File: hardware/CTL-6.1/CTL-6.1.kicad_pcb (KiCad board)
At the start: 2 copper layers, 107.6 x 45.1 mm, 79 parts, among them J1 Conn_02x16_Top_Bottom, J3 Conn_01x03, J4 Conn_01x03, J5 Conn_02x06_Odd_Even, J6 Conn_01x04, J7 Conn_01x04, K1 G5V-1, Q1 BCX56, Q2 BCX56, Q3 BCX56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

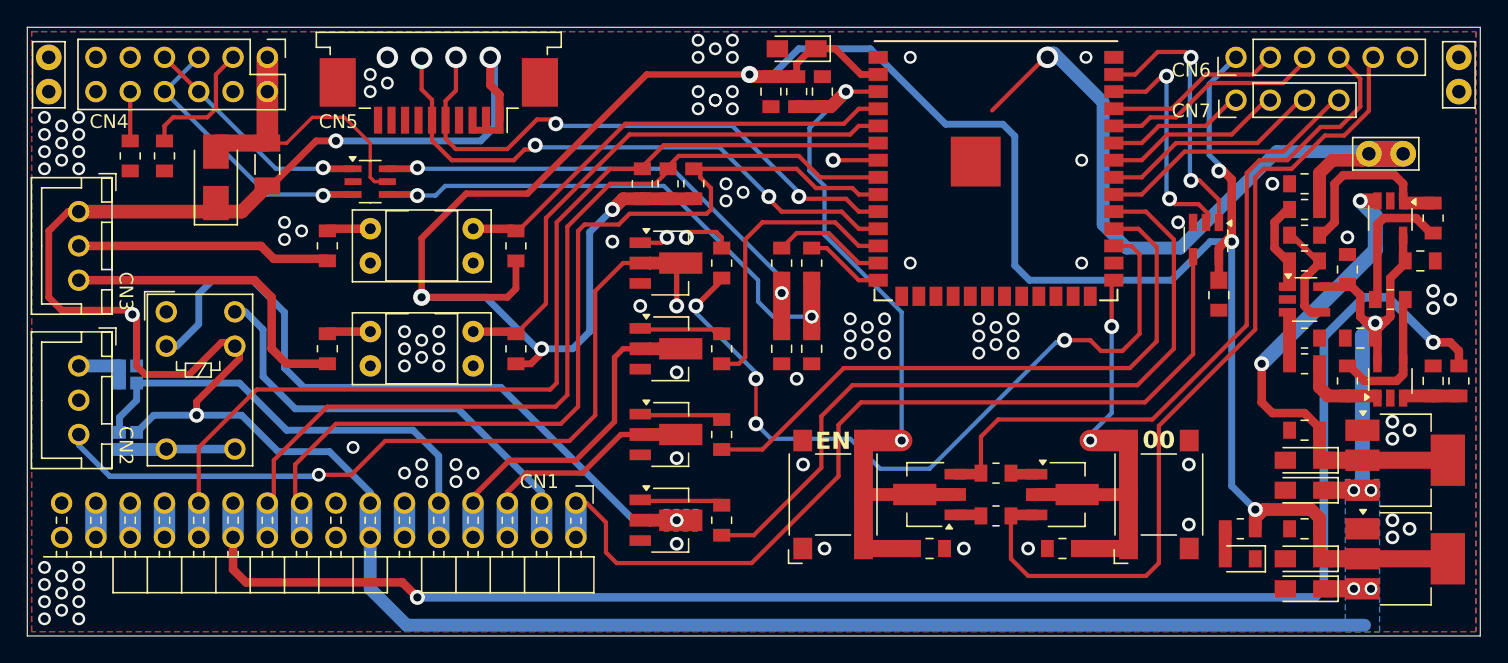
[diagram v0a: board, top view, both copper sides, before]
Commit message: modified:   .DS_Store 	new file:   archive/DL5NEG - Low Cost RF Power Sensor.xlsx 	renamed:    archive/Purchase 20260209/Invoice | Tokopedia 1.pdf -> archive/Purchase 20260209/Invoice - Tokopedia 1.pdf 	renamed:    archive/Purchase 20260209/Invoice | Tokopedia 2.pdf -> archive/Purchase 20260209/Invoice - Tokopedia 2.pdf 	renamed:    archive/Purchase 20260209/Invoice | Tokopedia 3.pdf -> archive/Purchase 20260209/Invoice - Tokopedia 3.pdf 	renamed:    archive/Purchase 20260209/Invoice | Tokopedia 4.pdf -> archive/Purchase 20260209/Invoice - Tokopedia 4.pdf 	renamed:    archive/Purchase 20260209/Invoice | Tokopedia 5.pdf -> archive/Purchase 20260209/Invoice - Tokopedia 5.pdf 	new file:   hardware/CTL-6.1/CTL-6.1-backups/CTL-6.1-2026-05-22_160447.zip 	new file:   hardware/CTL-6.1/CTL-6.1-backups/CTL-6.1-2026-05-22_160956.zip 	new file:   hardware/CTL-6.1/CTL-6.1-backups/CTL-6.1-2026-05-22_162109.zip 	new file:   hardware/CTL-6.1/CTL-6.1-backups/CTL-6.1-2026-05-22_163223.zip 	new file:   hardware/CTL-6.1/CTL-6.1-backups/CTL-6.1-2026-05-22_210324.zip 	new file:   hardware/CTL-6.1/CTL-6.1-backups/CTL-6.1-2026-05-25_112244.zip 	modified:   hardware/CTL-6.1/CTL-6.1.kicad_pcb 	modified:   hardware/CTL-6.1/CTL-6.1.kicad_pro
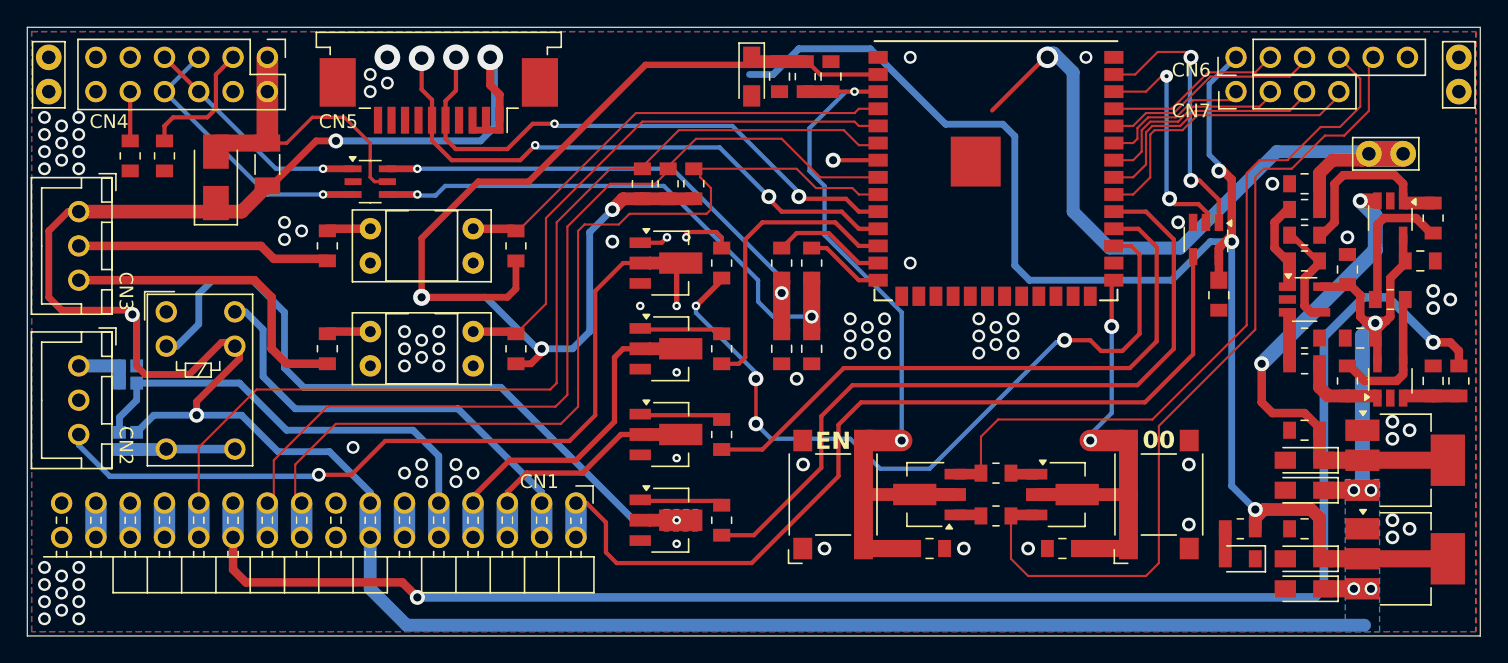
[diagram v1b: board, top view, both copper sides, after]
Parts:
- moved C10 3.92 mm to (98.1, 64.9), turned to -90 degrees
- moved C11 1.28 mm to (100.2, 64.9)
- moved C9 1.28 mm to (104.0, 64.9)
- moved R16 1.28 mm to (102.1, 64.9)
- moved J7 0.63 mm to (134.0, 66.0)
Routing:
- net +3.3V: track 195.4 -> 193.2 mm, vias 7 -> 6
- net /TCK: track 19.5 -> 21.4 mm
- net /TDO: track 16.5 -> 17.9 mm
- net /EN: track 57.3 -> 56.2 mm
- net /MSD2: track 68.5 -> 69.5 mm
- net /TDI: track 13.4 -> 14.3 mm
- net /OPTO: track 73.2 -> 74.1 mm
- net /REM: track 57.2 -> 58.0 mm
- net GND: vias 103 -> 87

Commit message: new file:   hardware/CTL-6.0/CTL-6.0-backups/CTL-6.0-2026-06-11_110233.zip 	modified:   hardware/CTL-6.0/CTL-6.0.kicad_prl 	modified:   hardware/CTL-6.0/CTL-6.0.kicad_pro 	deleted:    hardware/CTL-6.1/CTL-6.1-backups/CTL-6.1-2026-05-21_160708.zip 	deleted:    hardware/CTL-6.1/CTL-6.1-backups/CTL-6.1-2026-05-21_163235.zip 	deleted:    hardware/CTL-6.1/CTL-6.1-backups/CTL-6.1-2026-05-22_160447.zip 	deleted:    hardware/CTL-6.1/CTL-6.1-backups/CTL-6.1-2026-05-22_160956.zip 	deleted:    hardware/CTL-6.1/CTL-6.1-backups/CTL-6.1-2026-05-22_162109.zip 	deleted:    hardware/CTL-6.1/CTL-6.1-backups/CTL-6.1-2026-05-22_163223.zip 	deleted:    hardware/CTL-6.1/CTL-6.1-backups/CTL-6.1-2026-05-22_210324.zip 	deleted:    hardware/CTL-6.1/CTL-6.1-backups/CTL-6.1-2026-05-25_112244.zip 	new file:   hardware/CTL-6.1/CTL-6.1-backups/CTL-6.1-2026-06-11_110530.zip 	new file:   hardware/CTL-6.1/CTL-6.1-backups/CTL-6.1-2026-06-11_110702.zip 	new file:   hardware/CTL-6.1/CTL-6.1-backups/CTL-6.1-2026-06-11_111015.zip 	new file:   hardware/CTL-6.1/CTL-6.1-backups/CTL-6.1-2026-06-11_111525.zip 	new file:   hardware/CTL-6.1/CTL-6.1-backups/CTL-6.1-2026-06-11_112032.zip 	new file:   hardware/CTL-6.1/CTL-6.1-backups/CTL-6.1-2026-06-11_112817.zip 	new file:   hardware/CTL-6.1/CTL-6.1-backups/CTL-6.1-2026-06-11_113247.zip 	new file:   hardware/CTL-6.1/CTL-6.1-backups/CTL-6.1-2026-06-11_115705.zip 	new file:   hardware/CTL-6.1/CTL-6.1-backups/CTL-6.1-2026-06-11_115856.zip 	modified:   hardware/CTL-6.1/CTL-6.1.kicad_pcb 	modified:   hardware/CTL-6.1/CTL-6.1.kicad_prl 	modified:   hardware/CTL-6.1/CTL-6.1.kicad_pro 	modified:   hardware/CTL-6.1/CTL-6.1.kicad_sch 	new file:   hardware/CTL-6.1/~CTL-6.1.kicad_pcb.lck 	new file:   hardware/CTL-6.1/~CTL-6.1.kicad_pro.lck 	new file:   hardware/CTL-6.1/~CTL-6.1.kicad_sch.lck
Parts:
- added R30: 3.3kΩ, Resistor_SMD:R_0805_2012Metric_Pad1.20x1.40mm_HandSolder, F.Cu at (139.1, 72.9)
- R29: value 10kΩ -> 1.8kΩ
- moved C19 9.63 mm to (148.6, 71.4), turned to -90 degrees
- moved C10 3.92 mm to (101.4, 62.9), turned to 180 degrees
- moved C11 1.28 mm to (99.5, 66.0)
- moved C9 1.28 mm to (103.3, 66.0)
- moved R16 1.28 mm to (101.4, 66.0)
- moved J7 0.63 mm to (134.0, 66.7)
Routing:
- net /OPTO: track 74.1 -> 85.8 mm, vias 0 -> 1
- net /SEN-COAG: track 40.1 -> 49.4 mm, vias 0 -> 1
- net /REM: track 58.0 -> 67.2 mm
- net /CTL-RLY-A.1: track 21.7 -> 29.2 mm, vias 0 -> 1
- net /SEN-CUT: track 33.5 -> 40.0 mm, vias 0 -> 1
- net /PWM.01: track 17.5 -> 23.6 mm, vias 2 -> 3
- net /CTL-PWM-EN: track 54.8 -> 60.8 mm, vias 0 -> 1
- net /PWM.00: track 20.1 -> 25.7 mm, vias 2 -> 3
- net /CTL-RLY-A.2: track 46.7 -> 52.2 mm, vias 0 -> 1
- net /CTL-BUZZ: track 56.3 -> 61.2 mm, vias 4 -> 5
- net /MSD1: track 69.6 -> 73.8 mm, vias 0 -> 1
- net /MSD2: track 69.5 -> 72.1 mm, vias 0 -> 1
- net +3.3V: track 193.2 -> 195.4 mm, vias 6 -> 7
- net /TCK: track 21.4 -> 19.5 mm
- net /TDO: track 17.9 -> 16.5 mm
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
